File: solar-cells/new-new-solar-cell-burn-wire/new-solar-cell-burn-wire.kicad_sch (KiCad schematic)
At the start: 27 parts, among them J1 Solar Cell, J2 Burn Wire

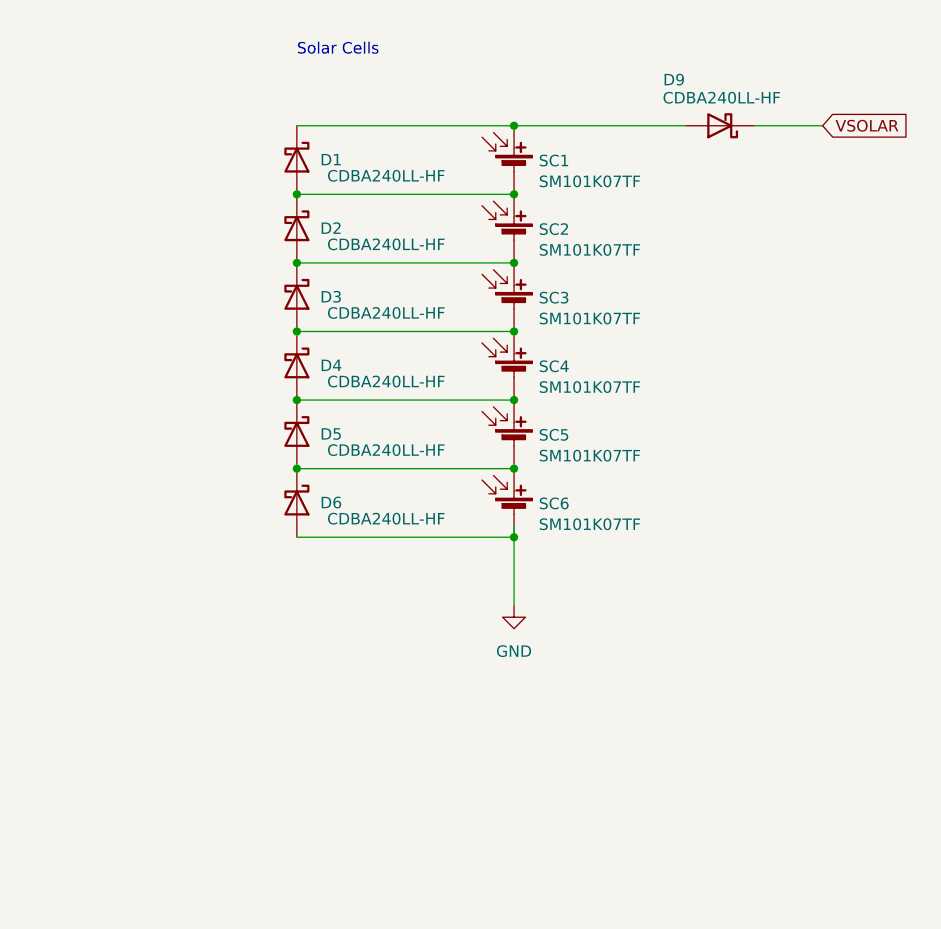
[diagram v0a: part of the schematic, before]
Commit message: changed burn wire to 3s2p config
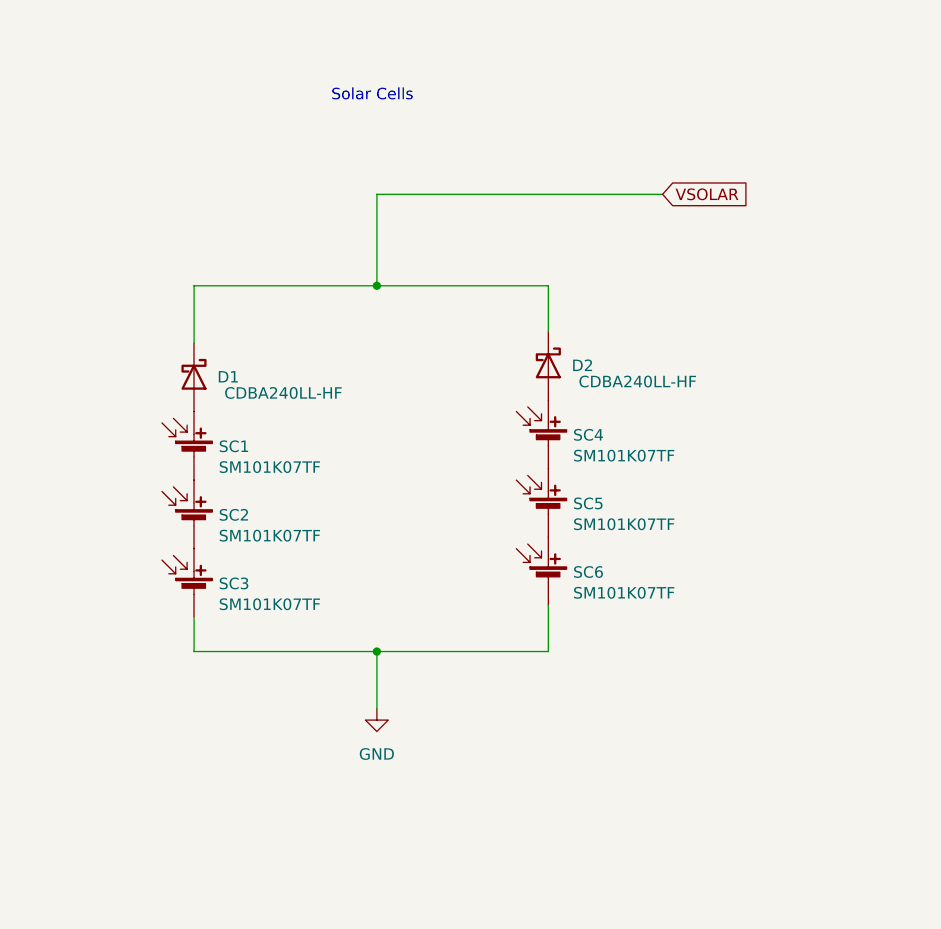
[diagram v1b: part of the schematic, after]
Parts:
- removed D3, D4, D5, D6, D9: CDBA240LL-HF, ISP:DO-214AC, symbol Device:D_Schottky
- renumbered SC4 to SC1, SC5 to SC2, SC6 to SC3, SC1 to SC4, SC2 to SC5, SC3 to SC6
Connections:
- net GND: now also SC6.2 (-)
- net VSOLAR: now also D1.1 (K), D2.1 (K)
- net at SC4.2 (-), SC5.1 (+): no longer D1.2 (A), D2.1 (K)
- net at SC5.2 (-), SC6.1 (+): no longer D2.2 (A)
- net at SC4.1 (+): now also D2.2 (A); no longer D1.1 (K)
- net at SC1.1 (+): now also D1.2 (A); no longer SC6.2 (-)
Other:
- moved on the sheet: SC1, SC2, SC3, SC4, SC5, SC6
